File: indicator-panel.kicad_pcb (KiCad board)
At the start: 2 copper layers, 133.1 x 77.2 mm, 85 parts, among them J101 Power In, P101 Data in, P102 Data Out, P103 Power In, P104 Power Out, U101 MAX3094E, U102 STP16CP05, U103 STP16CP05, U104 MAX3033E, U106 STP16CP05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

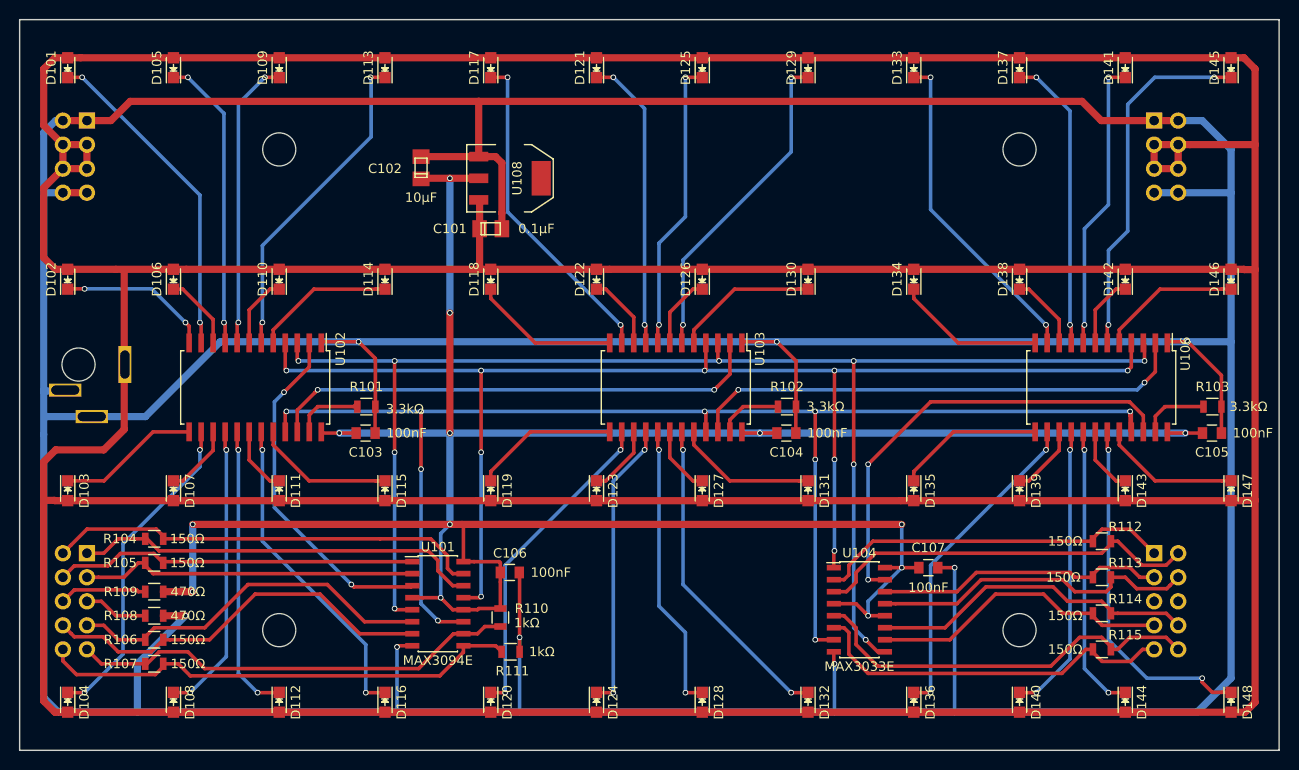
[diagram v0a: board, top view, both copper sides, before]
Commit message: Fix for correct spacing
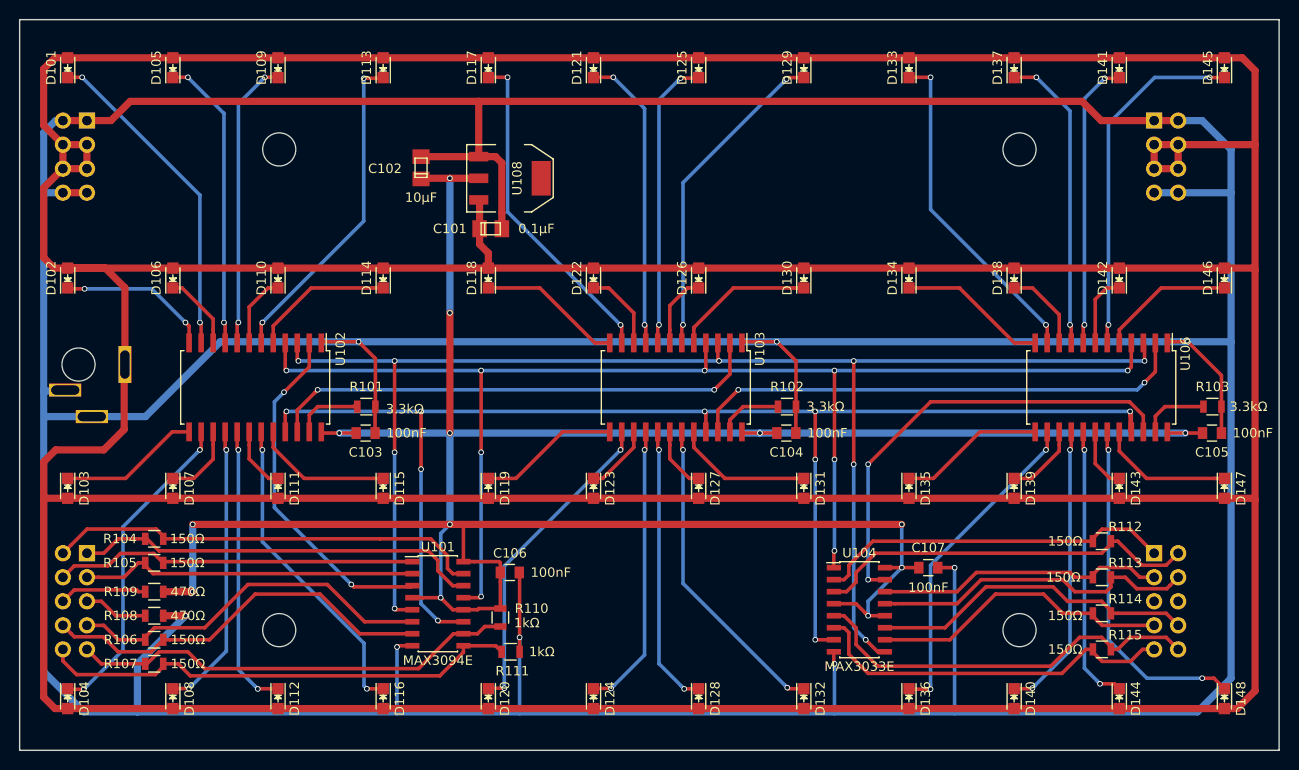
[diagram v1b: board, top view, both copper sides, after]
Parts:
- moved D148 0.80 mm to (183.7, 129.2)
- moved D147 0.74 mm to (183.7, 106.9)
- moved D144 0.74 mm to (172.6, 129.2)
- moved D146 0.71 mm to (183.7, 84.7)
- moved D145 0.70 mm to (183.7, 62.5)
- moved D140 0.69 mm to (161.5, 129.2)
- moved D143 0.68 mm to (172.6, 106.9)
- moved D142 0.65 mm to (172.6, 84.7)
- moved D141 0.64 mm to (172.6, 62.5)
- moved D136 0.64 mm to (150.4, 129.2)
- moved D139 0.63 mm to (161.5, 106.9)
- moved D138 0.59 mm to (161.5, 84.7)
- moved D132 0.59 mm to (139.3, 129.2)
- moved D137 0.57 mm to (161.5, 62.5)
- moved D135 0.57 mm to (150.4, 106.9)
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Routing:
- net +12V: track 688.5 -> 692.6 mm
- net GND: track 642.2 -> 640.6 mm
- net Net-(D148-Pad1): track 37.5 -> 36.4 mm
- net Net-(D138-Pad1): track 7.99 -> 8.92 mm
- net Net-(D144-Pad1): track 30.5 -> 29.6 mm
- net Net-(D128-Pad1): track 30.6 -> 29.9 mm
- net Net-(D145-Pad1): track 38.2 -> 37.5 mm
- net Net-(D132-Pad1): track 34.1 -> 33.4 mm
- net Net-(D116-Pad1): track 34.2 -> 33.5 mm
- net Net-(D146-Pad1): track 15.0 -> 14.3 mm
- net Net-(D122-Pad1): track 7.89 -> 8.52 mm
- net Net-(D137-Pad1): track 31.4 -> 32.0 mm
- net Net-(D112-Pad1): track 30.8 -> 30.2 mm
- net Net-(D143-Pad1): track 7.06 -> 6.55 mm
- net Net-(D133-Pad1): track 35.0 -> 35.5 mm
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
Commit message: Moved mounting holes to give a better attach point in the light shield
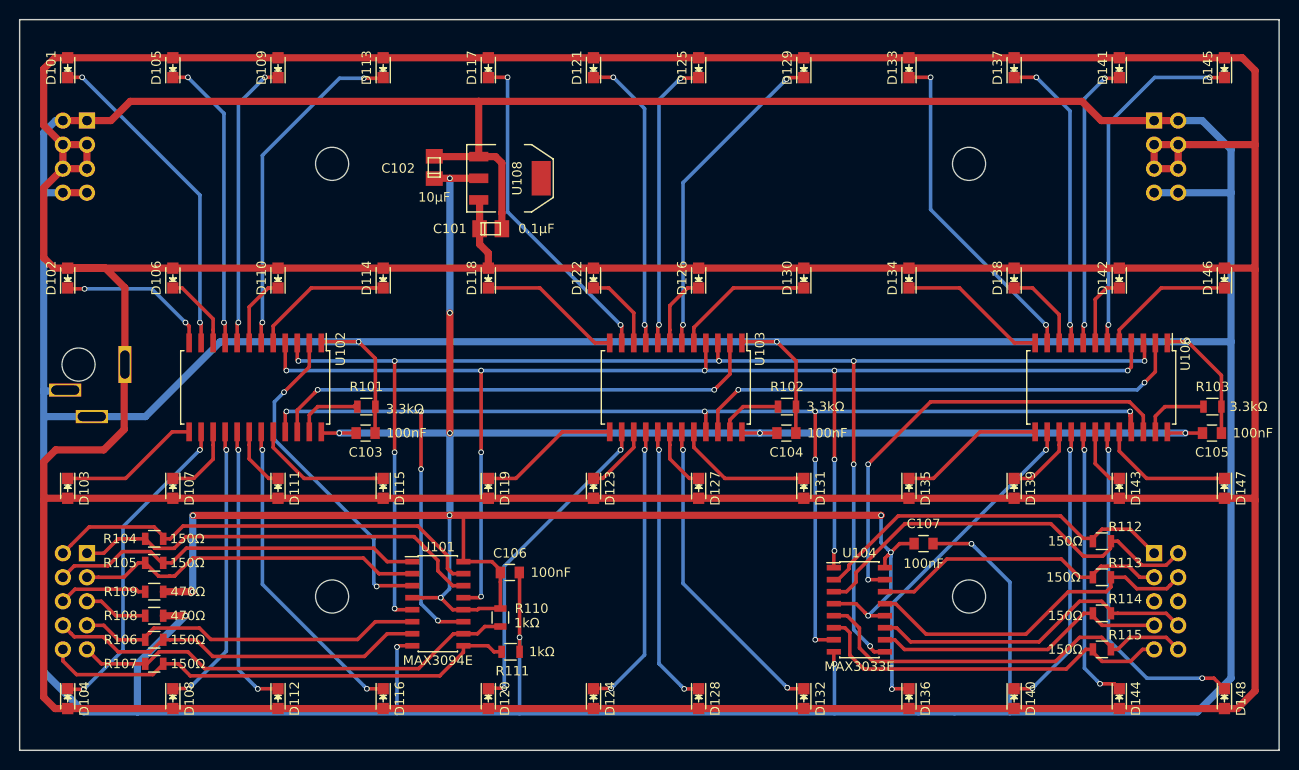
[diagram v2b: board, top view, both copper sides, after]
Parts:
- moved REF** 6.62 mm to (89.4, 118.4)
- moved REF** 6.41 mm to (156.7, 118.4)
- moved REF** 5.79 mm to (89.4, 72.6)
- moved REF** 5.55 mm to (156.7, 72.6)
- moved C107 2.59 mm to (151.9, 112.8)
- moved C102 1.40 mm to (100.2, 73.0)
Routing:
- net GND: track 640.6 -> 645.7 mm
- net Net-(P102-Pad2): track 40.9 -> 44.1 mm
- net Net-(P101-Pad7): track 39.2 -> 37.0 mm
- net Net-(P101-Pad8): track 42.3 -> 40.3 mm
- net Net-(P102-Pad1): track 37.9 -> 39.6 mm
- net Net-(P102-Pad4): track 34.8 -> 36.4 mm
- net Net-(D113-Pad1): track 34.5 -> 36.0 mm
- net Net-(U101-Pad3): track 37.0 -> 35.5 mm
- net Net-(P101-Pad3): track 35.7 -> 37.1 mm
- net Net-(P101-Pad4): track 38.4 -> 39.8 mm
- net Net-(P101-Pad2): track 46.3 -> 47.6 mm
- net Net-(P102-Pad3): track 30.5 -> 31.8 mm
- net Net-(D136-Pad1): track 34.6 -> 35.8 mm
- net Net-(P101-Pad1): track 43.1 -> 44.1 mm
- net Net-(P102-Pad7): track 32.0 -> 31.2 mm

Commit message: Make VDD and GND pins on chips visible.
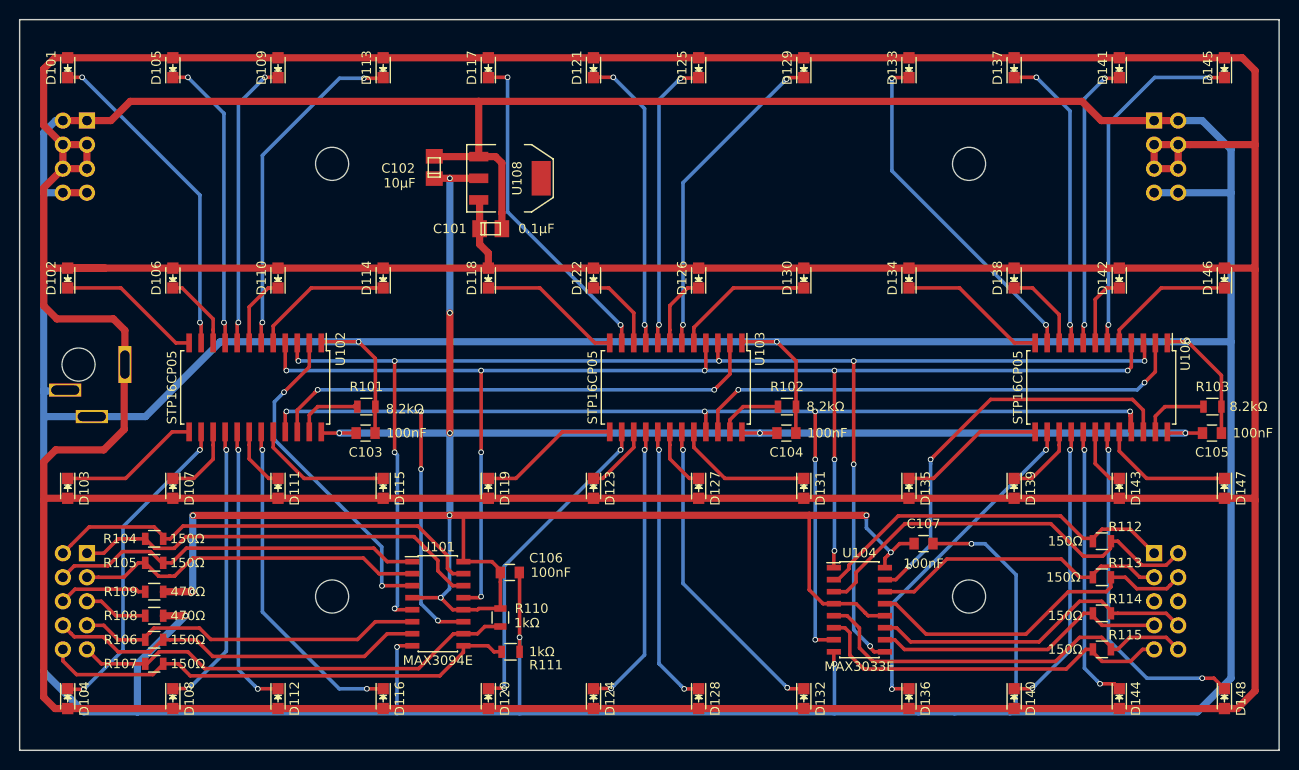
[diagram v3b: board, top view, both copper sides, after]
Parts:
- R101, R102, R103: value 3.3kΩ -> 8.2kΩ
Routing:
- net +12V: track 692.6 -> 699.4 mm
- net Net-(U104-Pad15): track 48.1 -> 43.2 mm
- net +3V3: track 279.8 -> 282.3 mm, vias 13 -> 12
- net GND: track 645.7 -> 647.5 mm
- net Net-(D116-Pad1): track 33.5 -> 35.2 mm
- net Net-(D133-Pad1): track 35.5 -> 36.6 mm
- net Net-(D102-Pad1): track 16.3 -> 15.4 mm, vias 2 -> 0

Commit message: Relocated coaxial power connector and increased pad size on its footprint.
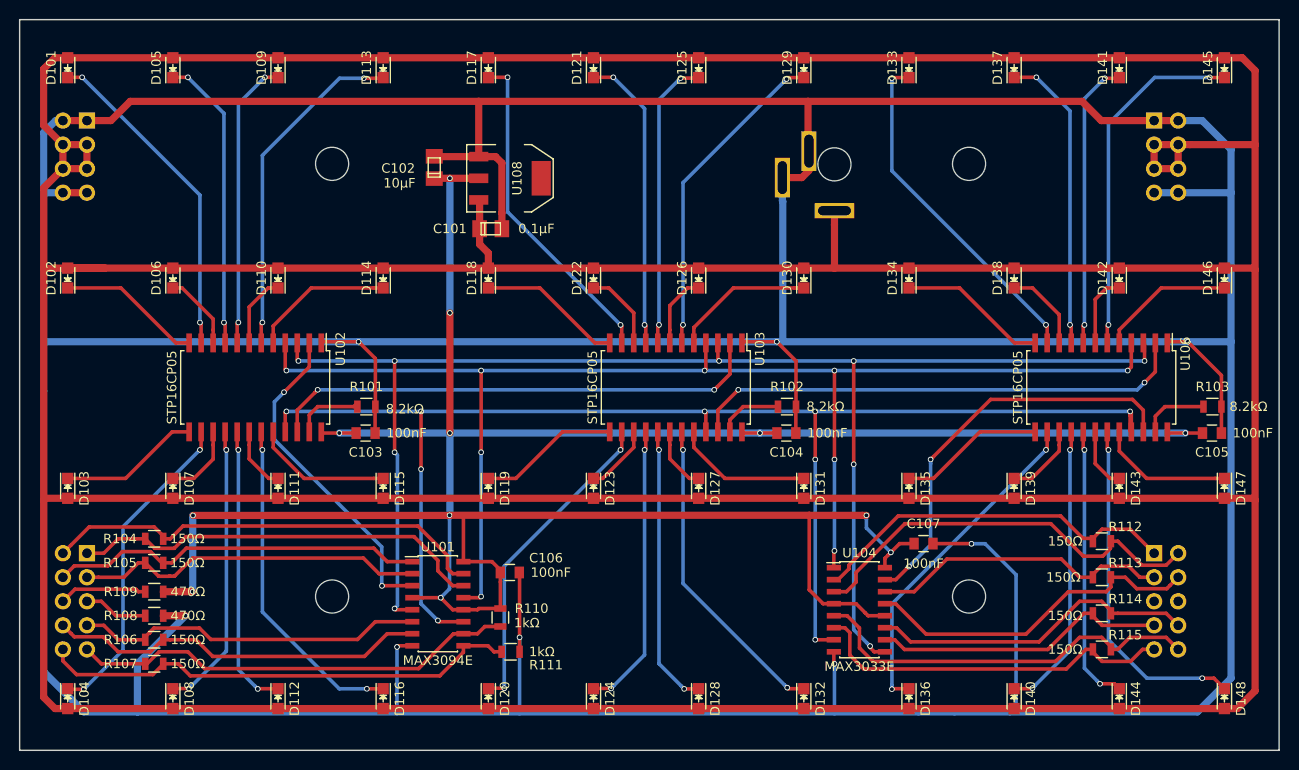
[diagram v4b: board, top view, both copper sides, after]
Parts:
- J101: footprint myMods.pretty:PJ-032B -> PJ-032B
- moved J101 76.7 mm to (142.5, 77.6), turned to 90 degrees
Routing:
- net GND: track 647.5 -> 669.8 mm
- net +12V: track 699.4 -> 691.8 mm

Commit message: Added fiducials and ground pads
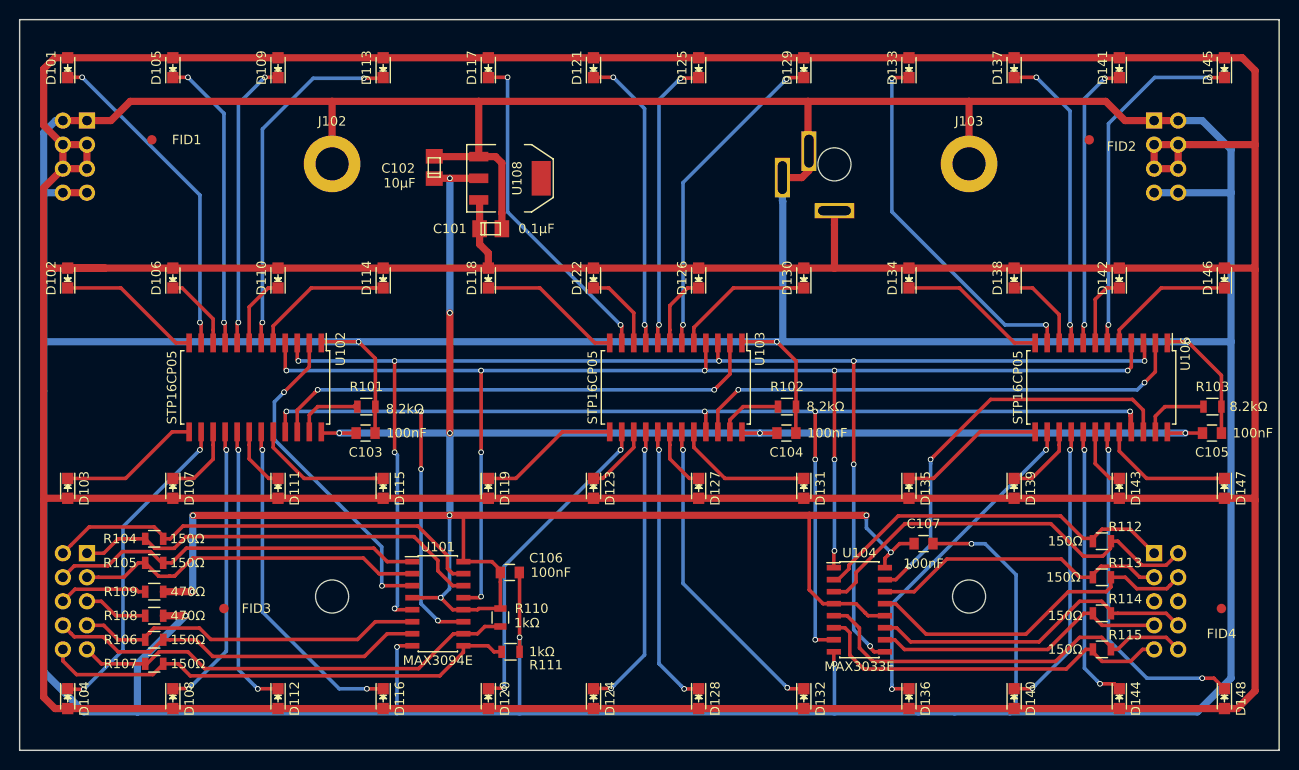
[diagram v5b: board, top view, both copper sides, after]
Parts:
- removed the REF** at (89.4, 72.6)
- removed the REF** at (156.7, 72.6)
- added FID1: Fiducial, Fiducials:Fiducial_1mm_Dia_2.54mm_Outer_CopperTop, F.Cu at (70.4, 70.1)
- added FID2: Fiducial, Fiducials:Fiducial_1mm_Dia_2.54mm_Outer_CopperTop, F.Cu at (169.4, 70.1)
- added FID3: Fiducial, Fiducials:Fiducial_1mm_Dia_2.54mm_Outer_CopperTop, F.Cu at (78.0, 119.6)
- added FID4: Fiducial, Fiducials:Fiducial_1mm_Dia_2.54mm_Outer_CopperTop, F.Cu at (183.4, 119.6)
- added J102: GND, Mounting_Holes:MountingHole_3-5mm, F.Cu at (89.4, 72.6)
- added J103: GND, Mounting_Holes:MountingHole_3-5mm, F.Cu at (156.7, 72.6)
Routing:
- net GND: track 669.8 -> 683.0 mm
- net Net-(D133-Pad1): track 36.6 -> 39.1 mm
- net Net-(D113-Pad1): track 36.0 -> 37.7 mm

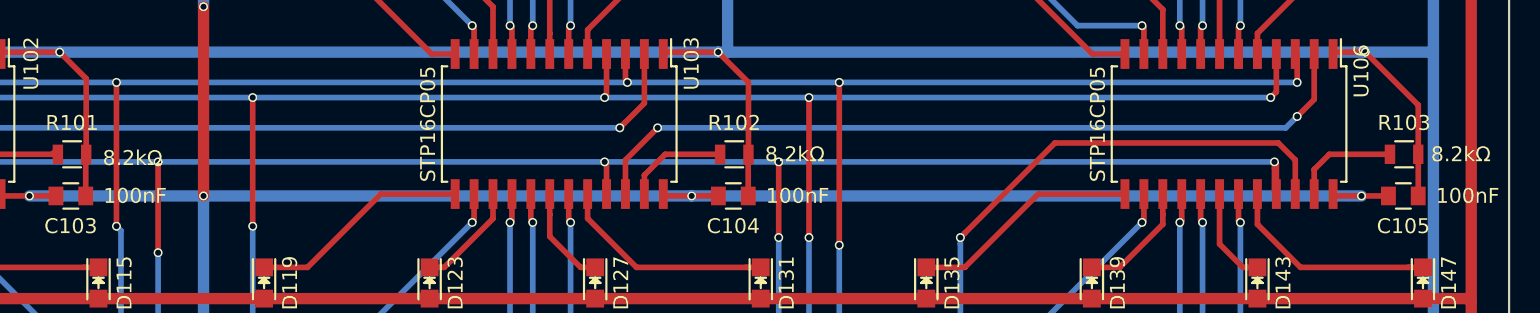
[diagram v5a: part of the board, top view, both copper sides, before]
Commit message: Changed current limiting resistor to 8.2k
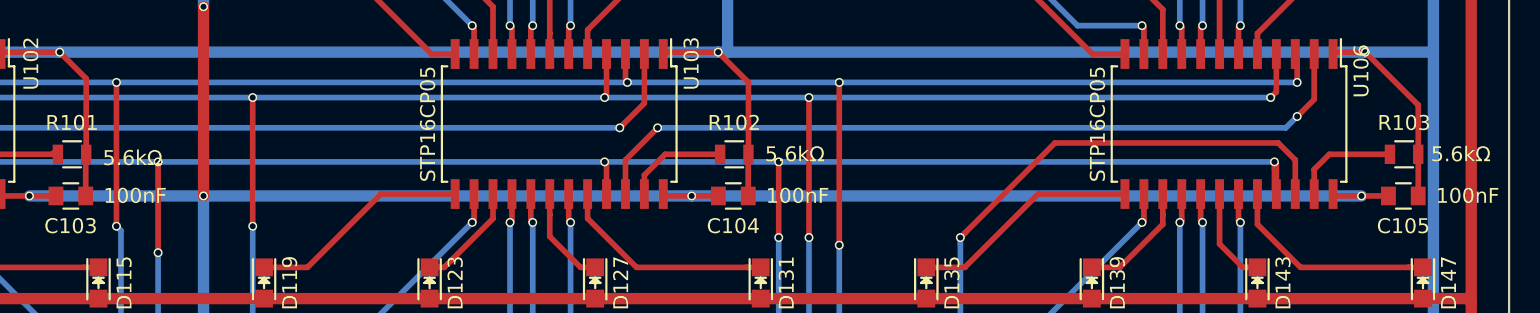
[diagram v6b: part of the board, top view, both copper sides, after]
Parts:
- R101, R102, R103: value 8.2kΩ -> 5.6kΩ
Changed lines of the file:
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@@
 (kicad_pcb (version 4) (host pcbnew 4.0.7+dfsg1-1)
   (general
-    (links 0)
-    (no_connects 2)
-    (area 50.122599 57.328999 189.603401 134.695001)
+    (links 207)
+    (no_connects 0)
+    (area 56.312999 57.328999 189.559001 134.695001)
     (thickness 1.6)
     (drawings 5)
@@
     (descr "Through hole pin header")
     (tags "pin header")
-    (fp_text reference P101 (at -4.826 -2.032 180) (layer B.SilkS)
+    (fp_text reference P101 (at -4.064 0.127 180) (layer B.SilkS)
       (effects (font (size 1 1) (thickness 0.15)) (justify mirror))
     )
@@
     (descr "Through hole socket strip")
     (tags "socket strip")
-    (fp_text reference P102 (at 1.524 4.826 360) (layer B.SilkS)
+    (fp_text reference P102 (at 0 4.445 360) (layer B.SilkS)
       (effects (font (size 1 1) (thickness 0.15)) (justify mirror))
     )
@@
     (descr "Through hole pin header")
     (tags "pin header")
-    (fp_text reference P103 (at -4.572 -0.508 180) (layer B.SilkS)
+    (fp_text reference P103 (at -4.064 0.889 180) (layer B.SilkS)
       (effects (font (size 1 1) (thickness 0.15)) (justify mirror))
     )
@@
     (descr "Through hole socket strip")
     (tags "socket strip")
-    (fp_text reference P104 (at 2.54 4.572 360) (layer B.SilkS)
+    (fp_text reference P104 (at 0 4.445 360) (layer B.SilkS)
       (effects (font (size 1 1) (thickness 0.15)) (justify mirror))
     )
-    (fp_text value "Power Out" (at 6.096 5.842 360) (layer B.SilkS)
+    (fp_text value "Power Out" (at 3.937 6.096 360) (layer B.SilkS)
       (effects (font (size 1 1) (thickness 0.15)) (justify mirror))
     )
@@
       (effects (font (size 1 1) (thickness 0.15)))
     )
-    (fp_text value 8.2kΩ (at 4.064 0.254) (layer F.SilkS)
+    (fp_text value 5.6kΩ (at 4.064 0.254) (layer F.SilkS)
       (effects (font (size 1 1) (thickness 0.15)))
     )
@@
       (effects (font (size 1 1) (thickness 0.15)))
     )
-    (fp_text value 8.2kΩ (at 4.064 0) (layer F.SilkS)
+    (fp_text value 5.6kΩ (at 4.064 0) (layer F.SilkS)
       (effects (font (size 1 1) (thickness 0.15)))
     )
@@
       (effects (font (size 1 1) (thickness 0.15)))
     )
-    (fp_text value 8.2kΩ (at 3.81 0) (layer F.SilkS)
-      (effects (font (size 1 1) (thickness 0.15)))
-    )
+    (fp_text value 5.6kΩ (at 3.81 0) (layer F.SilkS)
+      (effects (font (size 1 1) (thickness 0.15)))
+    )
